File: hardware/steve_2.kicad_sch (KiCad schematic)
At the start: 32 parts, among them J4 TerminalBlock_1770979_4pos_Ve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, J6 MicroSD_Hirose_DM3AT, J7 TerminalBlock_1770885_2pos, Q1 Q_NMOS_GSD, U4 BMI270, U5 BMP388/390

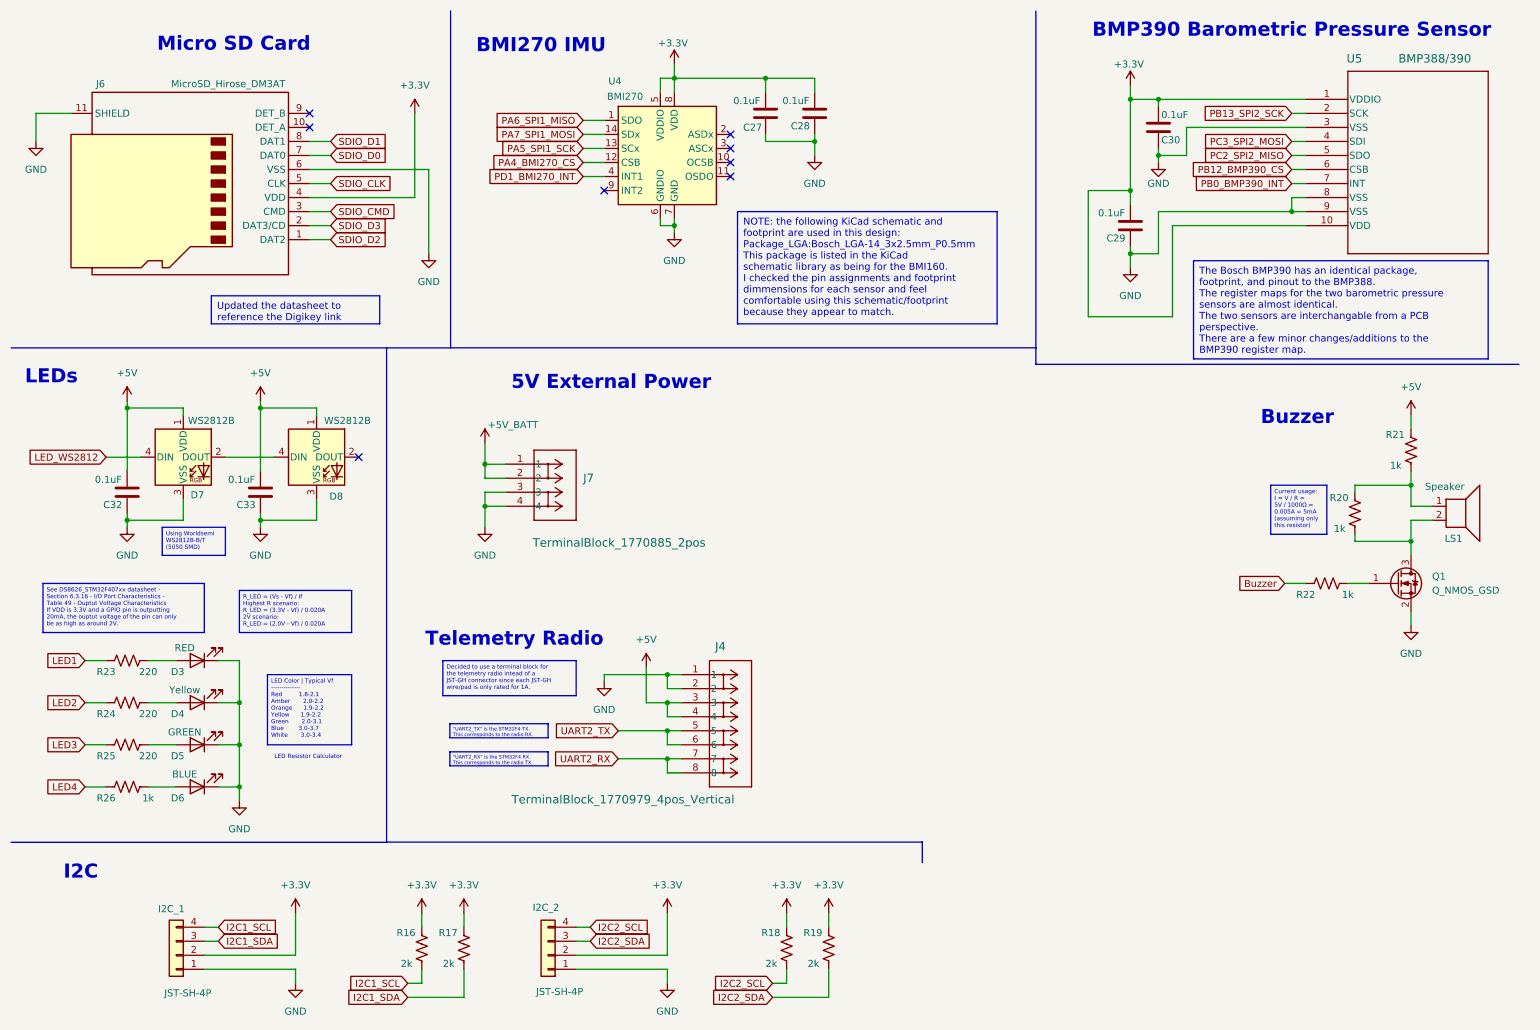
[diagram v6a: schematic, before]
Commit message: started component layout
started component layout - attempting to use a 60x60mm board size
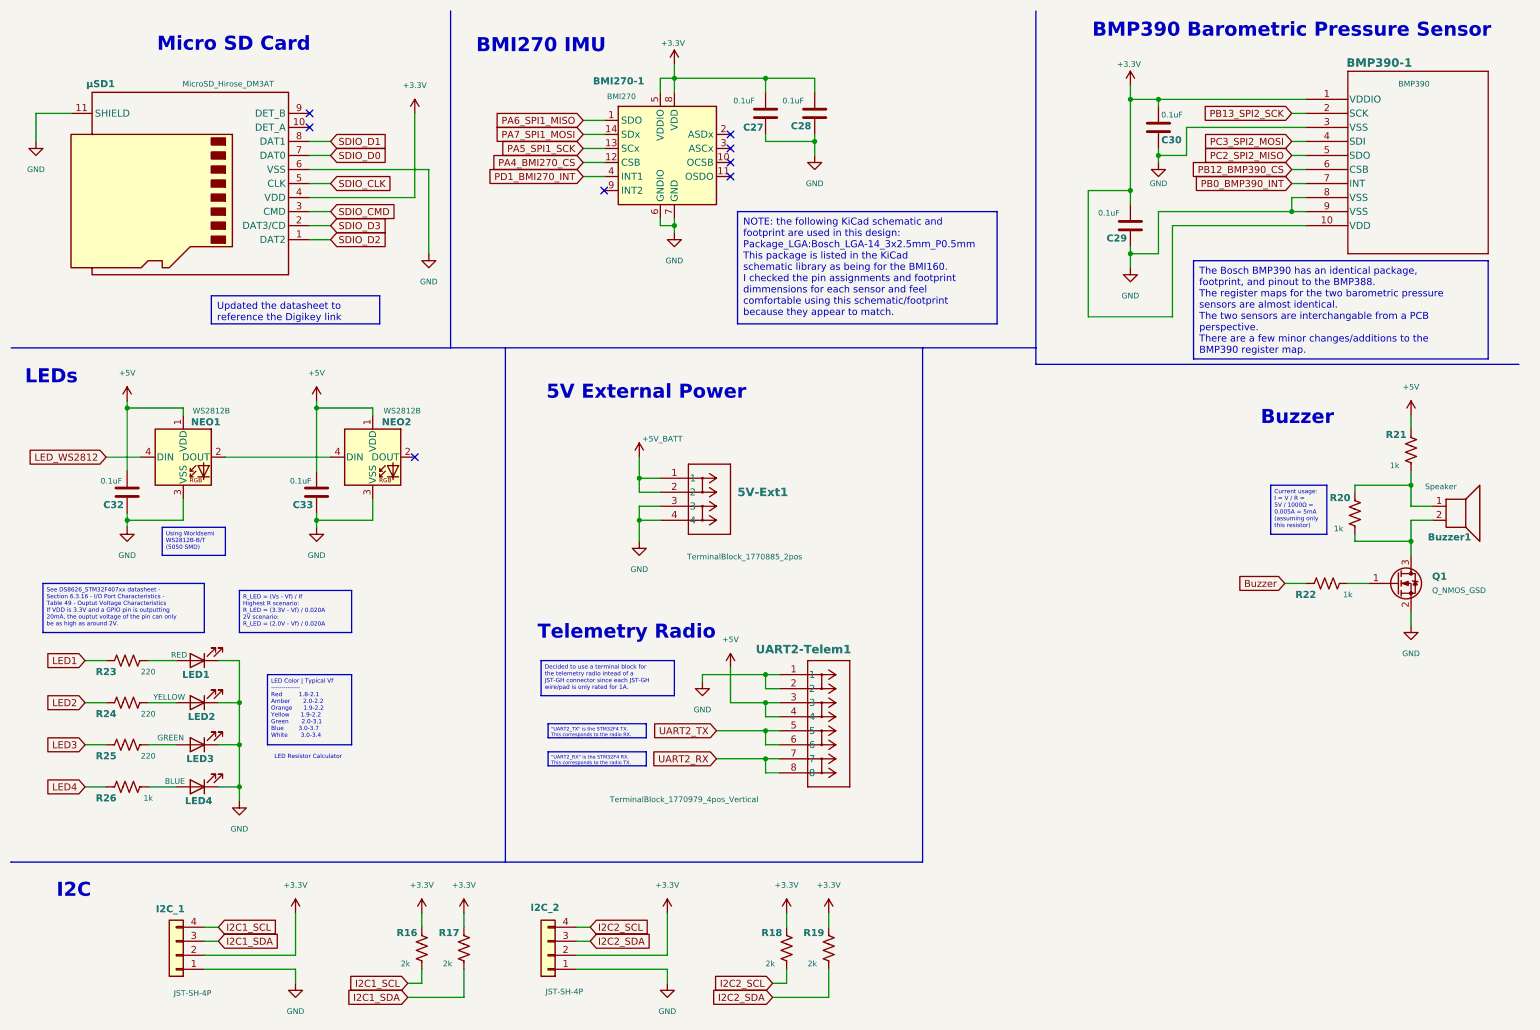
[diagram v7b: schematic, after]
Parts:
- BMP390-1: renamed from U5; value BMP388/390 -> BMP390
- LED2: renamed from D4; value Yellow -> YELLOW
- renumbered J7 to 5V-Ext1, U4 to BMI270-1, LS1 to Buzzer1, D3 to LED1, D5 to LED3, D6 to LED4, D7 to NEO1, D8 to NEO2, J4 to UART2-Telem1, J6 to µSD1
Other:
- moved on the sheet: 5V-Ext1, C33, NEO2, UART2-Telem1
